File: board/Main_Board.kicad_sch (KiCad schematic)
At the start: 19 parts, among them J1 X Axis Encoder, J2 J2 Encoder, J3 J3 Encoder, J4 J4 Encoder, J5 Pitch Encoder, J6 I2C Bus, SW1 Enable Switch, U1 Teensy4.1_DEV-16771

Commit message: Complete main board pre-review
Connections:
- net AE1: now also U1.27 (A13); no longer U1.14 (A0)
- net AE2: now also U1.26 (A12); no longer U1.15 (A1)
- net AE3: now also U1.25 (A11); no longer U1.16 (A2)
- net AE4: now also U1.24 (A10); no longer U1.17 (A3)
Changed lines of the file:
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@@
-	)
-	(no_connect
-		(at 198.12 120.65)
 	)
 	(no_connect
@@
 	)
 	(no_connect
+		(at 157.48 115.57)
+	)
+	(no_connect
 		(at 157.48 105.41)
 	)
 	(no_connect
+		(at 157.48 113.03)
+	)
+	(no_connect
 		(at 157.48 72.39)
 	)
@@
 	)
 	(no_connect
-		(at 198.12 123.19)
-	)
-	(no_connect
 		(at 157.48 69.85)
 	)
@@
 	)
 	(no_connect
+		(at 157.48 118.11)
+	)
+	(no_connect
 		(at 198.12 46.99)
 	)
 	(no_connect
-		(at 198.12 125.73)
-	)
-	(no_connect
 		(at 157.48 102.87)
 	)
@@
 	)
 	(no_connect
-		(at 198.12 128.27)
+		(at 157.48 110.49)
 	)
 	(wire
@@
 	(global_label "AE2"
 		(shape input)
-		(at 157.48 113.03 180)
-		(fields_autoplaced yes)
-		(effects
-			(font
-				(size 1.27 1.27)
-			)
-			(justify right)
-		)
-		(property "Intersheetrefs" "${INTERSHEET_REFS}"
-			(at 151.0477 113.03 0)
-			(effects
-				(font
-					(size 1.27 1.27)
-				)
-				(justify right)
+		(at 198.12 123.19 0)
+		(fields_autoplaced yes)
+		(effects
+			(font
+				(size 1.27 1.27)
+			)
+			(justify left)
+		)
+		(property "Intersheetrefs" "${INTERSHEET_REFS}"
+			(at 204.5523 123.19 0)
+			(effects
+				(font
+					(size 1.27 1.27)
+				)
+				(justify left)
 				(hide yes)
 			)
@@
 	(global_label "AE4"
 		(shape input)
-		(at 157.48 118.11 180)
-		(fields_autoplaced yes)
-		(effects
-			(font
-				(size 1.27 1.27)
-			)
-			(justify right)
-		)
-		(property "Intersheetrefs" "${INTERSHEET_REFS}"
-			(at 151.0477 118.11 0)
-			(effects
-				(font
-					(size 1.27 1.27)
-				)
-				(justify right)
+		(at 198.12 128.27 0)
+		(fields_autoplaced yes)
+		(effects
+			(font
+				(size 1.27 1.27)
+			)
+			(justify left)
+		)
+		(property "Intersheetrefs" "${INTERSHEET_REFS}"
+			(at 204.5523 128.27 0)
+			(effects
+				(font
+					(size 1.27 1.27)
+				)
+				(justify left)
 				(hide yes)
 			)
@@
 	(global_label "AE1"
 		(shape input)
-		(at 157.48 110.49 180)
-		(fields_autoplaced yes)
-		(effects
-			(font
-				(size 1.27 1.27)
-			)
-			(justify right)
-		)
-		(property "Intersheetrefs" "${INTERSHEET_REFS}"
-			(at 151.0477 110.49 0)
-			(effects
-				(font
-					(size 1.27 1.27)
-				)
-				(justify right)
+		(at 198.12 120.65 0)
+		(fields_autoplaced yes)
+		(effects
+			(font
+				(size 1.27 1.27)
+			)
+			(justify left)
+		)
+		(property "Intersheetrefs" "${INTERSHEET_REFS}"
+			(at 204.5523 120.65 0)
+			(effects
+				(font
+					(size 1.27 1.27)
+				)
+				(justify left)
 				(hide yes)
 			)
@@
 	(global_label "AE3"
 		(shape input)
-		(at 157.48 115.57 180)
-		(fields_autoplaced yes)
-		(effects
-			(font
-				(size 1.27 1.27)
-			)
-			(justify right)
-		)
-		(property "Intersheetrefs" "${INTERSHEET_REFS}"
-			(at 151.0477 115.57 0)
-			(effects
-				(font
-					(size 1.27 1.27)
-				)
-				(justify right)
-				(hide yes)
-			)
+		(at 198.12 125.73 0)
+		(fields_autoplaced yes)
+		(effects
+			(font
+				(size 1.27 1.27)
+			)
+			(justify left)
+		)
+		(property "Intersheetrefs" "${INTERSHEET_REFS}"
+			(at 204.5523 125.73 0)
+			(effects
+				(font
+					(size 1.27 1.27)
+				)
+				(justify left)
+				(hide yes)
+			)

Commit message: Fixed via heart being too close together
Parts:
- U1: footprint MRDT_Shields:Teensy_4_1_Bare -> MODULE_DEV-16771
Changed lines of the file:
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@@
 			)
 		)
-		(property "Footprint" "MRDT_Shields:Teensy_4_1_Bare"
+		(property "Footprint" "MODULE_DEV-16771"
 			(at 231.14 97.79 0)
 			(effects

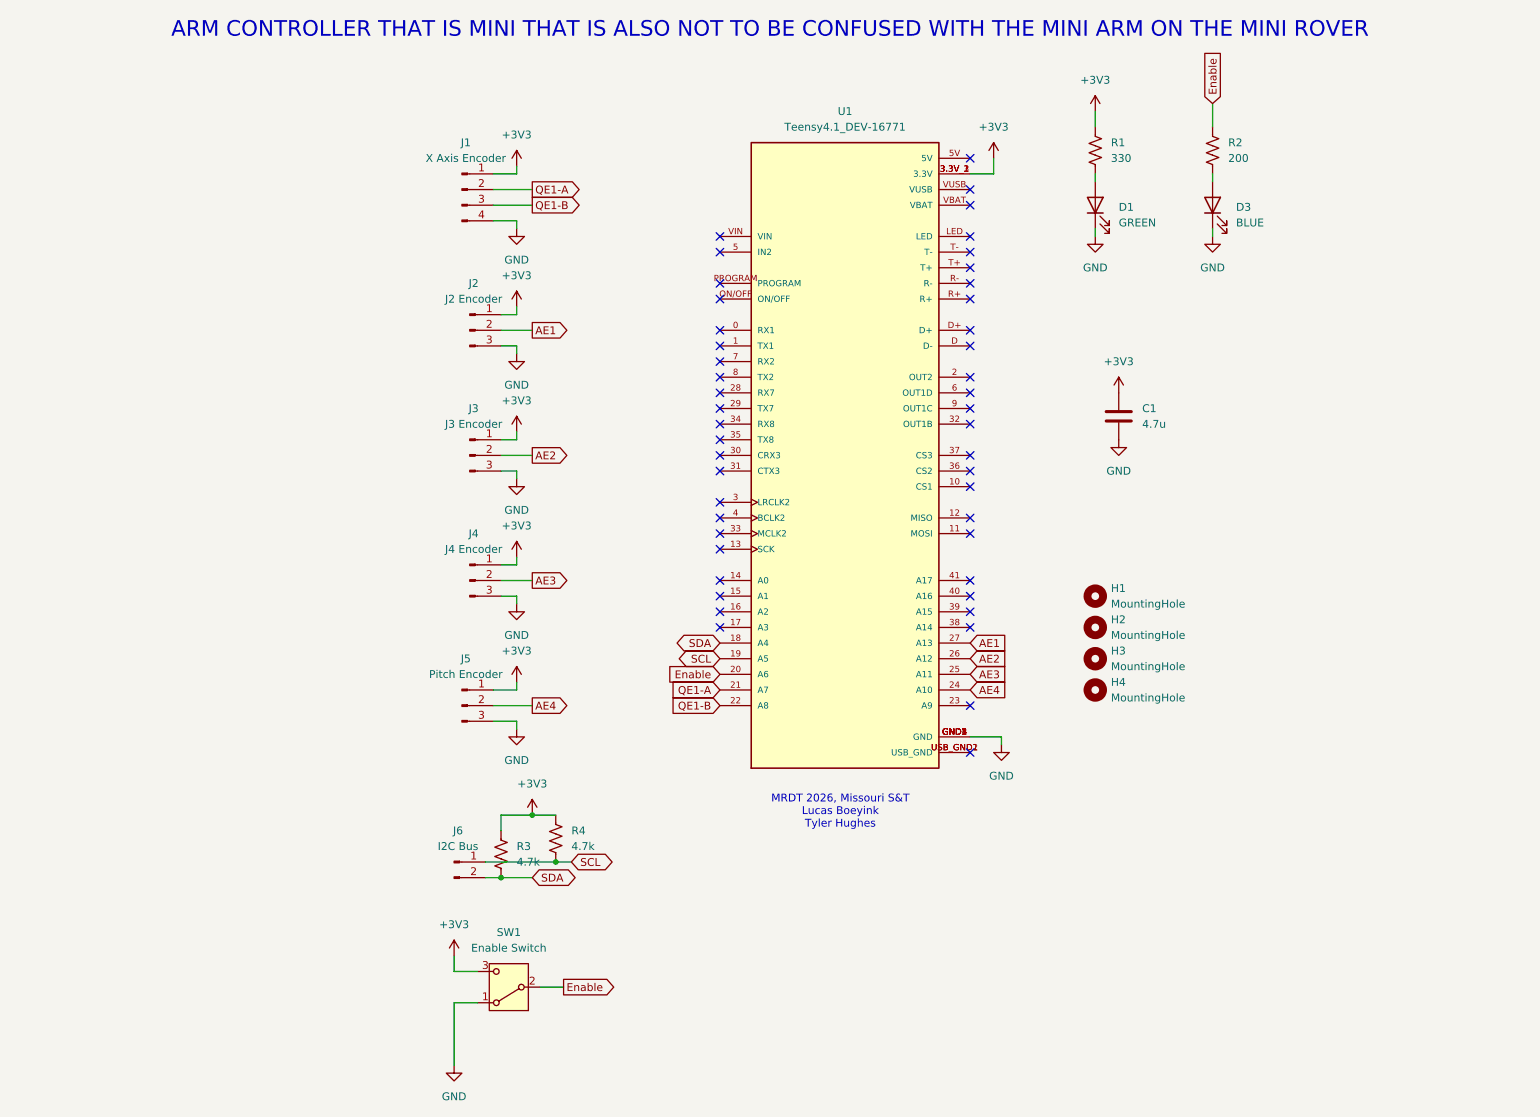
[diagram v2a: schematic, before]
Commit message: Add gripper and roll buttons
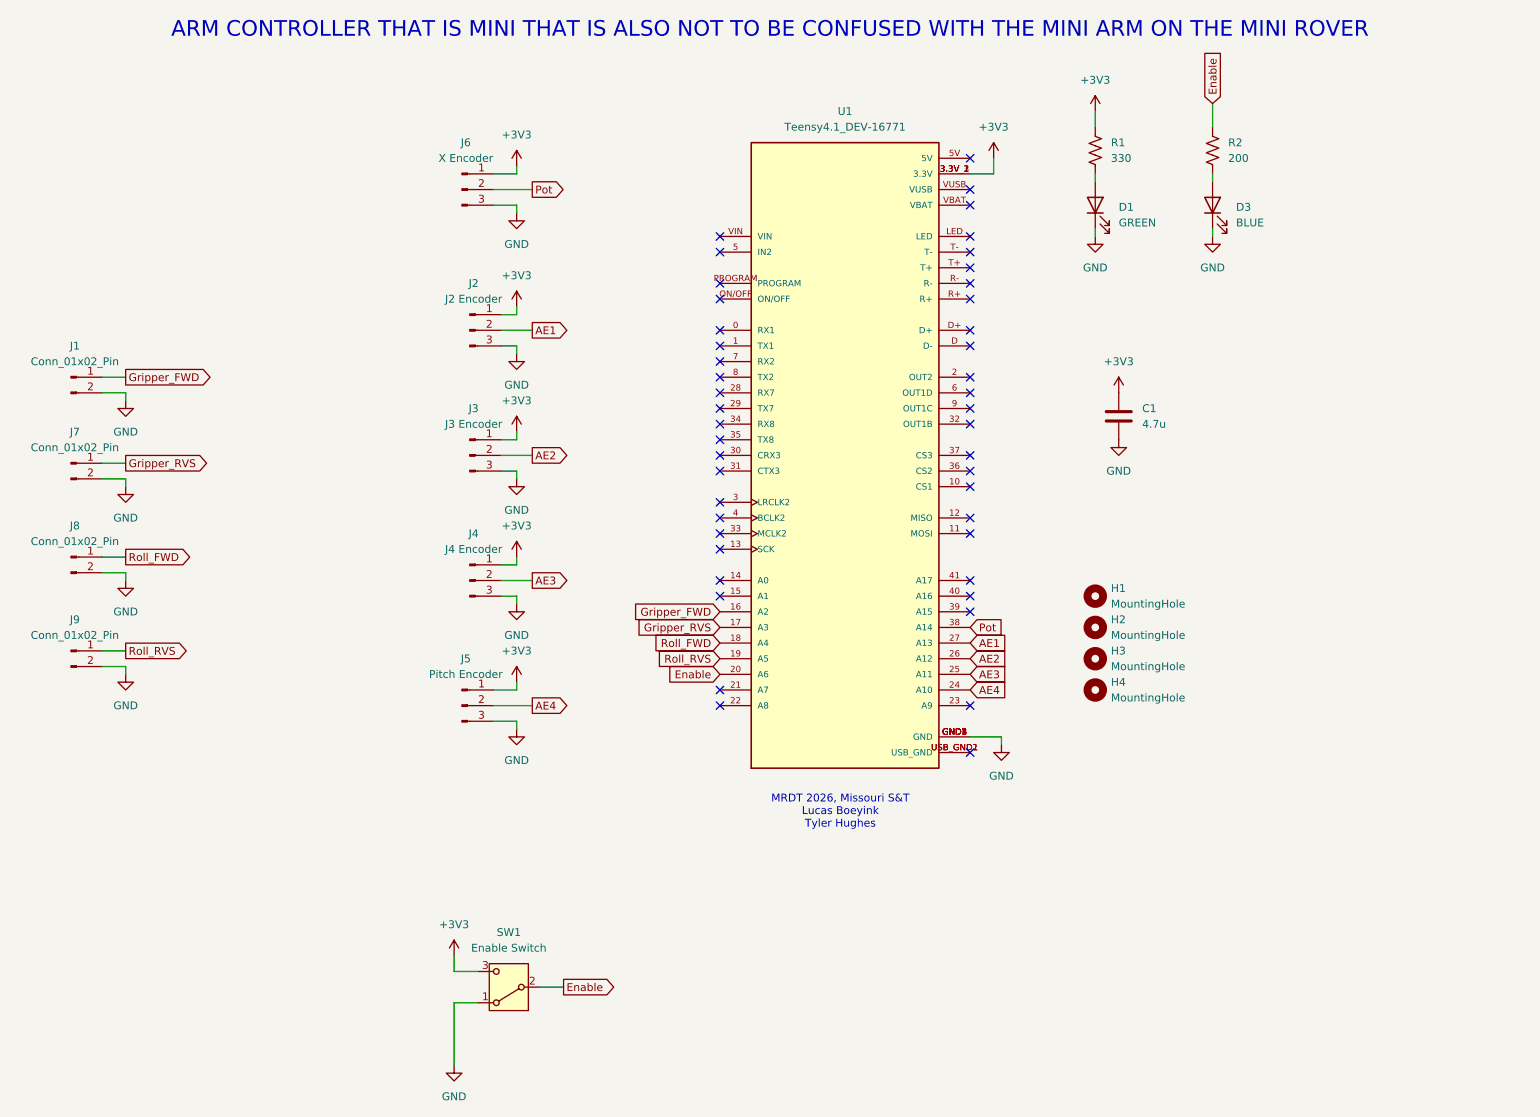
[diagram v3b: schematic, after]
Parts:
- removed J1: X Axis Encoder, Connector_JST:JST_PH_B4B-PH-K_1x04_P2.00mm_Vertical, symbol Connector:Conn_01x04_Pin
- removed J6: I2C Bus, Connector_JST:JST_PH_B2B-PH-K_1x02_P2.00mm_Vertical, symbol Connector:Conn_01x02_Pin
- removed R3, R4: 4.7k, Resistor_SMD:R_0603_1608Metric_Pad0.98x0.95mm_HandSolder, symbol Device:R_US
- added J1, J7, J8, J9: Conn_01x02_Pin, Connector_JST:JST_PH_B2B-PH-K_1x02_P2.00mm_Vertical, symbol Connector:Conn_01x02_Pin
- added J6: X Encoder, Connector_JST:JST_PH_B3B-PH-K_1x03_P2.00mm_Vertical, symbol Connector:Conn_01x03_Pin
- U1: footprint MODULE_DEV-16771 -> MRDT_Shields:Teensy_4_1_Bare
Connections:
- net +3V3: now also J6.1 (Pin_1)
- net GND: now also J1.2 (Pin_2), J6.3 (Pin_3), J7.2 (Pin_2), J8.2 (Pin_2), J9.2 (Pin_2)
- net Gripper_FWD: now reaches U1.16 (A2)
- net Gripper_FWD: now also J1.1 (Pin_1)
- net Gripper_RVS: now reaches U1.17 (A3)
- net Gripper_RVS: now also J7.1 (Pin_1)
- net Pot: now reaches U1.38 (A14)
- net Pot: now also J6.2 (Pin_2)
- net QE1-A: no longer names the net of U1.21 (A7)
- net QE1-B: no longer names the net of U1.22 (A8)
- net SCL renamed Roll_RVS
- net Roll_RVS: now also J9.1 (Pin_1)
- net SDA renamed Roll_FWD
- net Roll_FWD: now also J8.1 (Pin_1)
- no-connect marks 47 -> 46

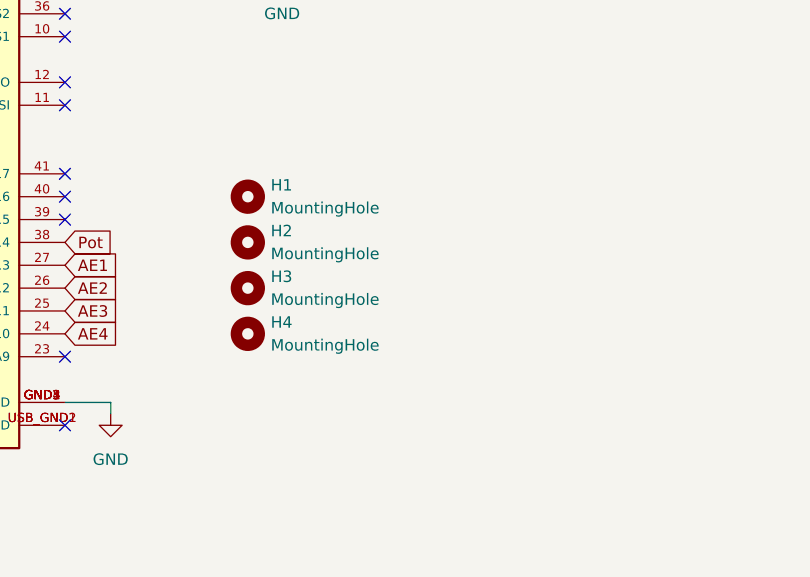
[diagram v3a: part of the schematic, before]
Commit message: Add plated mounting holes
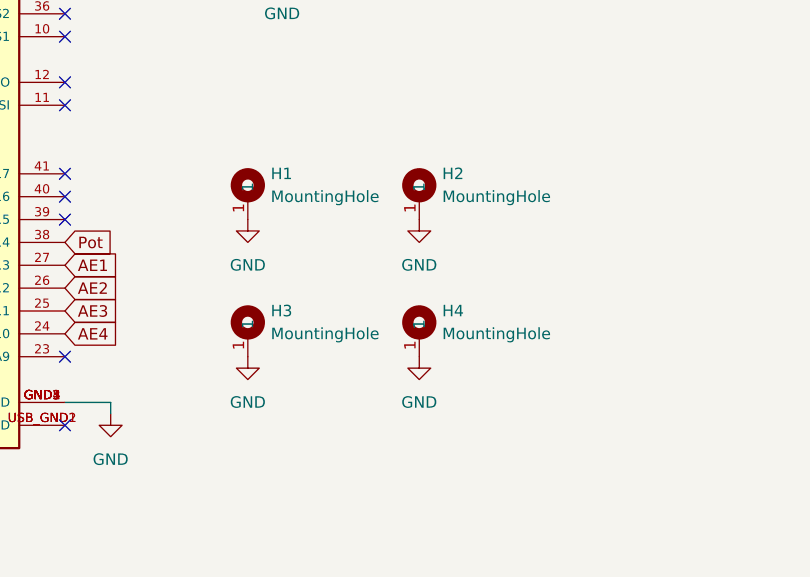
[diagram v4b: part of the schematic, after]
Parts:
- H1, H2, H3, H4: footprint MRDT_Drill_Holes:4_40_Hole -> MRDT_Drill_Holes:4_40_Hole_Pad_Via; symbol Mechanical:MountingHole -> MRDT_Connectors:4_40_Mounting_Hole_Pad; now in the parts list
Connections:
- net GND: now also H1.1, H2.1, H3.1, H4.1
